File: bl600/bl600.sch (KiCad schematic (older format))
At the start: 27 parts, among them IC1 BL600, IC2 LK112, P1 CONN_4, P2 CONN_3X2, P4 CONN_2, P5 CONN_8, P6 CONN_8, P7 CONN_6X2, Q1 MOSFET_P, Q2 MOSFET_P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

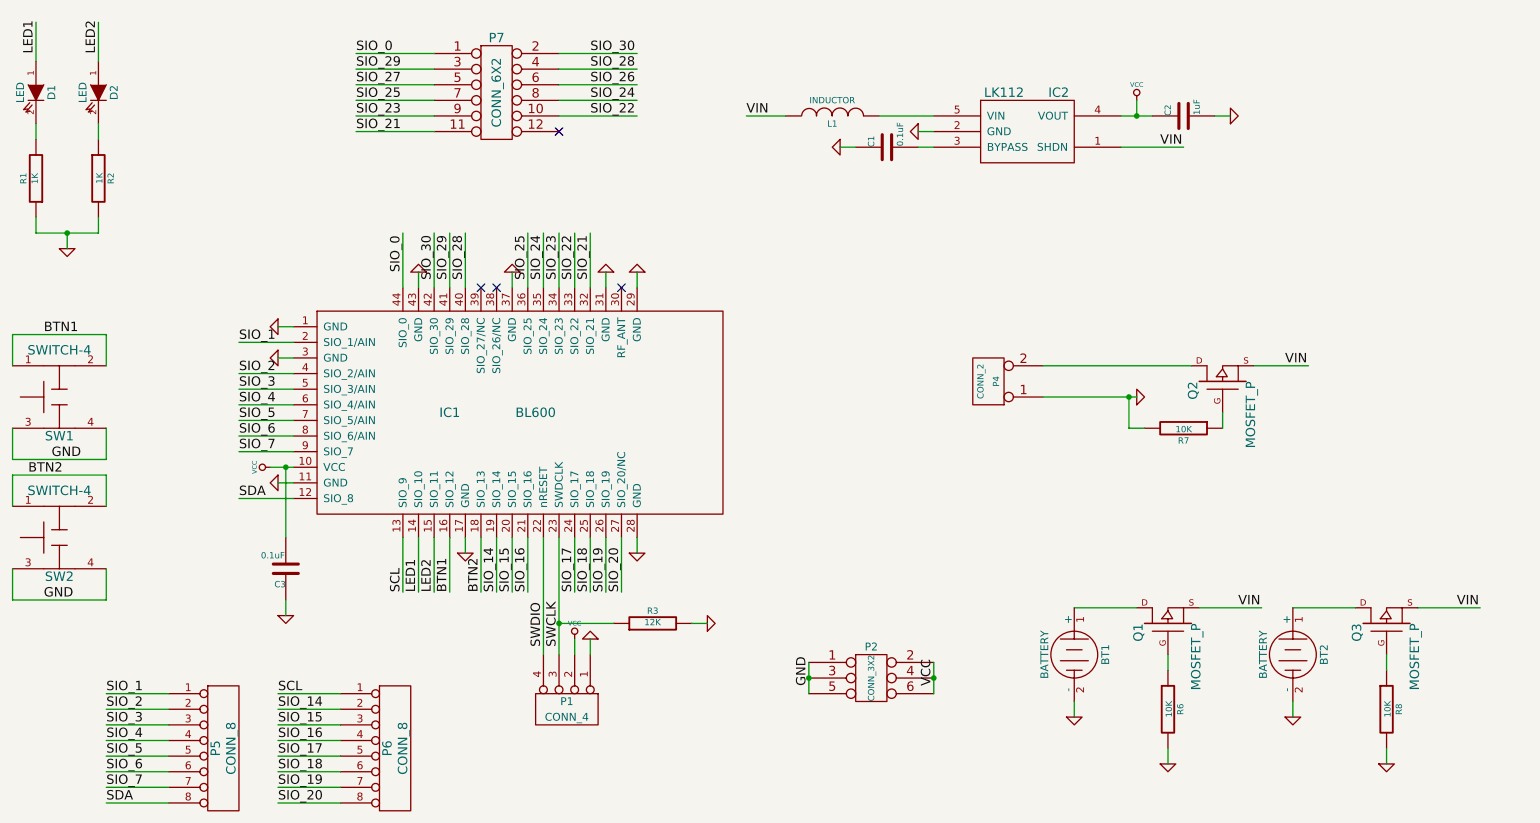
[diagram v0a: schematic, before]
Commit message: BL600 add ARM 10/9 pin SWD header
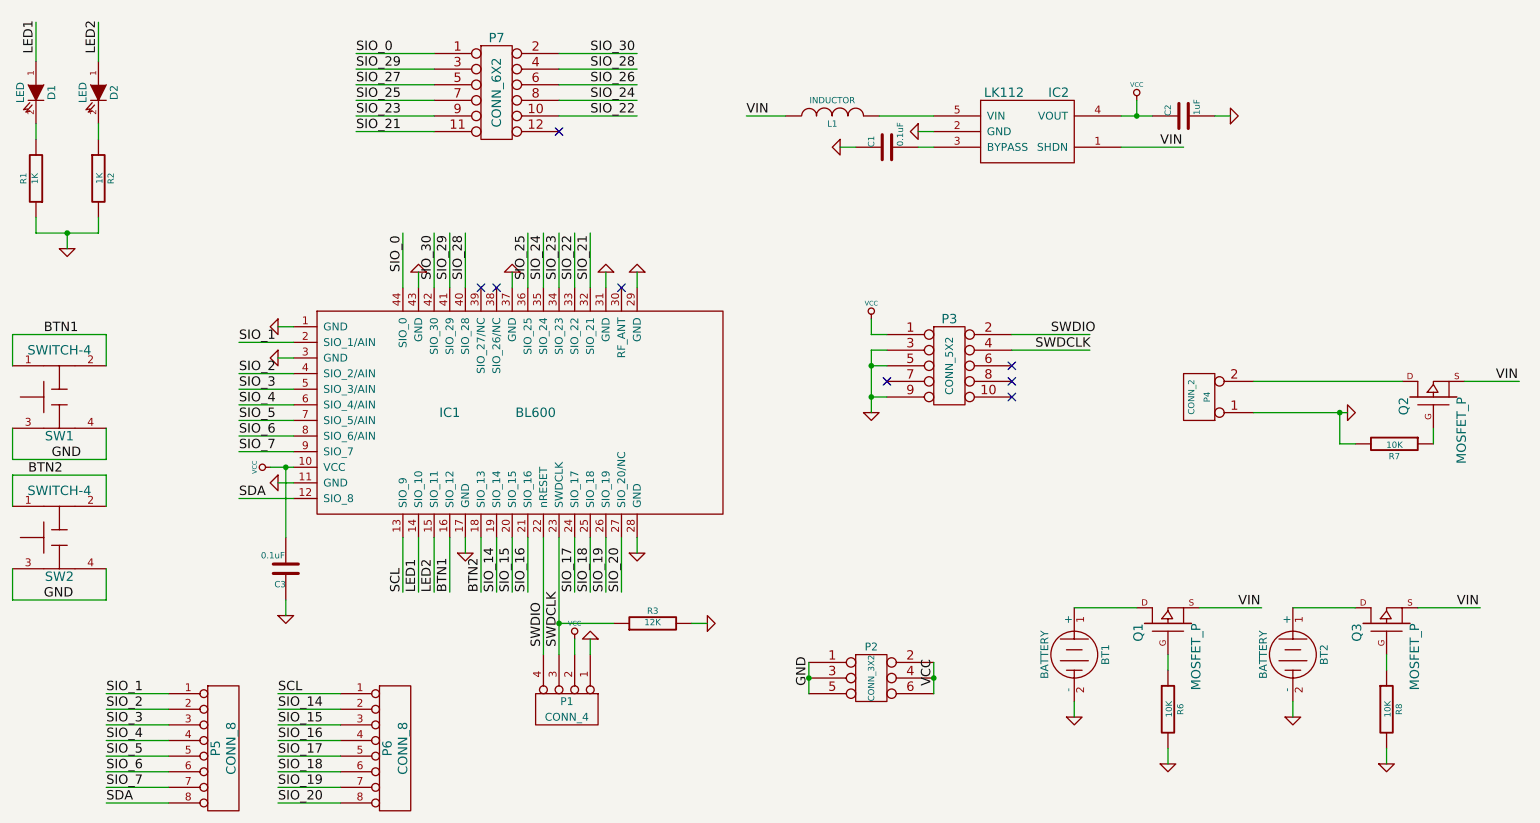
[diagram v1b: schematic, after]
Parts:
- added P3: CONN_5X2, ~, symbol CONN_5X2
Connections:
- net labels added: SWDCLK
- net labels removed: SWCLK
- wire segments 121 -> 129
- no-connect marks 4 -> 8
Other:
- moved on the sheet: P4, Q2, R7
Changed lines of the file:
@@
-EESchema Schematic File Version 2  date Thu 09 May 2013 07:33:31 AM EDT
+EESchema Schematic File Version 2  date Fri 10 May 2013 12:45:30 PM EDT
 LIBS:guan
 LIBS:power
@@
 Sheet 1 1
 Title ""
-Date "13 may 2013"
+Date "10 may 2013"
 Rev ""
 Comp ""
@@
 SWDIO
 Text Label 4700 5200 1    60   ~ 0
-SWCLK
+SWDCLK
 $Comp
 L VCC #PWR09
@@
 L CONN_2 P4
 U 1 1 518C10E5
-P 7450 3500
-F 0 "P4" V 7400 3500 40  0000 C CNN
-F 1 "CONN_2" V 7500 3500 40  0000 C CNN
-F 2 "~" H 7450 3500 60  0000 C CNN
-F 3 "~" H 7450 3500 60  0000 C CNN
-	1    7450 3500
+P 8800 3600
+F 0 "P4" V 8750 3600 40  0000 C CNN
+F 1 "CONN_2" V 8850 3600 40  0000 C CNN
+F 2 "~" H 8800 3600 60  0000 C CNN
+F 3 "~" H 8800 3600 60  0000 C CNN
+	1    8800 3600
 	-1   0    0    1
 $EndComp
@@
 L MOSFET_P Q2
 U 1 1 518C1103
-P 8950 3500
-F 0 "Q2" H 8950 3690 60  0000 R CNN
-F 1 "MOSFET_P" H 8950 3320 60  0000 R CNN
-F 2 "~" H 8950 3500 60  0000 C CNN
-F 3 "~" H 8950 3500 60  0000 C CNN
-	1    8950 3500
+P 10300 3600
+F 0 "Q2" H 10300 3790 60  0000 R CNN
+F 1 "MOSFET_P" H 10300 3420 60  0000 R CNN
+F 2 "~" H 10300 3600 60  0000 C CNN
+F 3 "~" H 10300 3600 60  0000 C CNN
+	1    10300 3600
 	0    -1   -1   0
 $EndComp
-Text Label 9350 3400 0    60   ~ 0
+Text Label 10700 3500 0    60   ~ 0
 VIN
 $Comp
 L GND #PWR014
 U 1 1 518C1EEF
-P 8400 3600
-F 0 "#PWR014" H 8400 3600 30  0001 C CNN
-F 1 "GND" H 8400 3530 30  0001 C CNN
-F 2 "" H 8400 3600 60  0000 C CNN
-F 3 "" H 8400 3600 60  0000 C CNN
-	1    8400 3600
+P 9750 3700
+F 0 "#PWR014" H 9750 3700 30  0001 C CNN
+F 1 "GND" H 9750 3630 30  0001 C CNN
+F 2 "" H 9750 3700 60  0000 C CNN
+F 3 "" H 9750 3700 60  0000 C CNN
+	1    9750 3700
 	0    -1   -1   0
 $EndComp
@@
 L R R7
 U 1 1 518C1F18
-P 8700 3800
-F 0 "R7" V 8780 3800 40  0000 C CNN
-F 1 "10K" V 8707 3801 40  0000 C CNN
-F 2 "~" V 8630 3800 30  0000 C CNN
-F 3 "~" H 8700 3800 30  0000 C CNN
-	1    8700 3800
+P 10050 3900
+F 0 "R7" V 10130 3900 40  0000 C CNN
+F 1 "10K" V 10057 3901 40  0000 C CNN
+F 2 "~" V 9980 3900 30  0000 C CNN
+F 3 "~" H 10050 3900 30  0000 C CNN
+	1    10050 3900
 	0    1    1    0
 $EndComp
@@
 	8000 5650 8000 5550
 Wire Wire Line
-	7800 3400 8750 3400
-Wire Wire Line
-	9150 3400 9500 3400
-Wire Wire Line
-	7800 3600 8400 3600
-Wire Wire Line
-	8950 3700 8950 3800
-Wire Wire Line
-	8450 3800 8350 3800
-Wire Wire Line
-	8350 3800 8350 3600
-Connection ~ 8350 3600
+	9150 3500 10100 3500
+Wire Wire Line
+	10500 3500 10850 3500
+Wire Wire Line
+	9150 3700 9750 3700
+Wire Wire Line
+	10300 3800 10300 3900
+Wire Wire Line
+	9800 3900 9700 3900
+Wire Wire Line
+	9700 3900 9700 3700
+Connection ~ 9700 3700
 Wire Wire Line
 	8000 4950 8400 4950
@@
 NoConn ~ 4200 2900
 NoConn ~ 4300 2900
+$Comp
+L CONN_5X2 P3
+U 1 1 518C242E
+P 7200 3400
+F 0 "P3" H 7200 3700 60  0000 C CNN
+F 1 "CONN_5X2" V 7200 3400 50  0000 C CNN
+F 2 "~" H 7200 3400 60  0000 C CNN
+F 3 "~" H 7200 3400 60  0000 C CNN
+	1    7200 3400
+	1    0    0    -1
+$EndComp
+$Comp
+L VCC #PWR025
+U 1 1 518C3106
+P 6700 3100
+F 0 "#PWR025" H 6700 3200 30  0001 C CNN
+F 1 "VCC" H 6700 3200 30  0000 C CNN
+F 2 "" H 6700 3100 60  0000 C CNN
+F 3 "" H 6700 3100 60  0000 C CNN
+	1    6700 3100
+	1    0    0    -1
+$EndComp
+Wire Wire Line
+	6700 3100 6700 3200
+Wire Wire Line
+	6700 3200 6800 3200
+$Comp
+L GND #PWR026
+U 1 1 518C3196
+P 6700 3700
+F 0 "#PWR026" H 6700 3700 30  0001 C CNN
+F 1 "GND" H 6700 3630 30  0001 C CNN
+F 2 "" H 6700 3700 60  0000 C CNN
+F 3 "" H 6700 3700 60  0000 C CNN
+	1    6700 3700
+	1    0    0    -1
+$EndComp
+Wire Wire Line
+	6700 3700 6700 3300
+Wire Wire Line
+	6700 3300 6800 3300
+Wire Wire Line
+	6800 3400 6700 3400
+Connection ~ 6700 3400
+Wire Wire Line
+	6800 3600 6700 3600
+Connection ~ 6700 3600
+NoConn ~ 6800 3500
+Wire Wire Line
+	7600 3200 8100 3200
+Wire Wire Line
+	8100 3300 7600 3300
+Text Label 7850 3200 0    60   ~ 0
+SWDIO
+Text Label 7750 3300 0    60   ~ 0
+SWDCLK
+NoConn ~ 7600 3400
+NoConn ~ 7600 3500
+NoConn ~ 7600 3600
 $EndSCHEMATC

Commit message: Connect CR2032 holder directly to 3V3
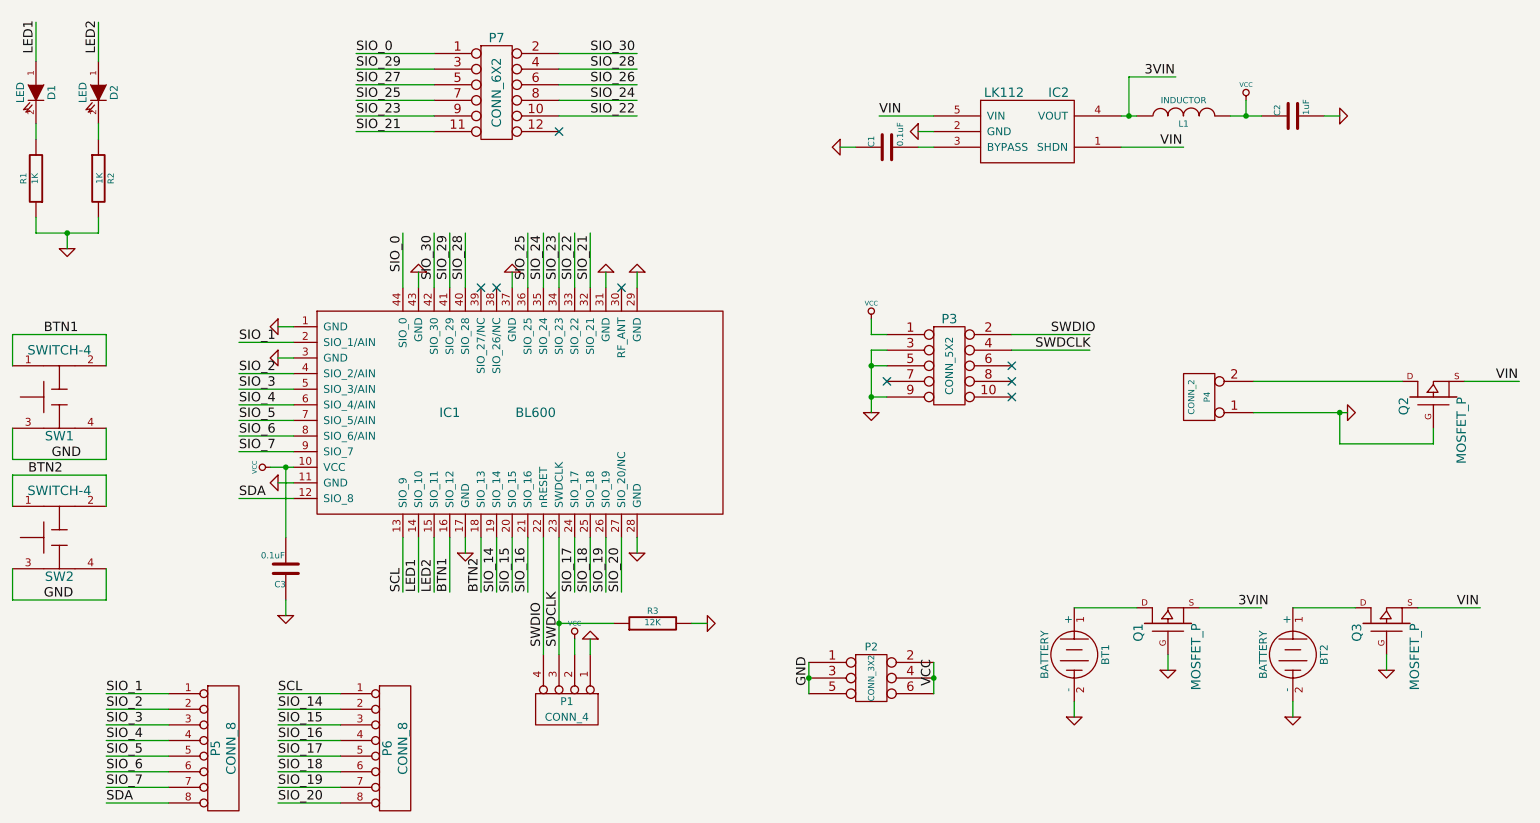
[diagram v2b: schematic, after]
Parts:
- removed R6, R7, R8: 10K, ~, symbol R
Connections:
- net labels added: 3VIN
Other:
- moved on the sheet: C2, L1
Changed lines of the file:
@@
-EESchema Schematic File Version 2  date Fri 10 May 2013 12:45:30 PM EDT
+EESchema Schematic File Version 2  date Tue 14 May 2013 06:35:55 AM EDT
 LIBS:guan
 LIBS:power
@@
 Sheet 1 1
 Title ""
-Date "10 may 2013"
+Date "14 may 2013"
 Rev ""
 Comp ""
@@
 $EndComp
 $Comp
-L R R7
-U 1 1 518C1F18
-P 10050 3900
-F 0 "R7" V 10130 3900 40  0000 C CNN
-F 1 "10K" V 10057 3901 40  0000 C CNN
-F 2 "~" V 9980 3900 30  0000 C CNN
-F 3 "~" H 10050 3900 30  0000 C CNN
-	1    10050 3900
-	0    1    1    0
-$EndComp
-$Comp
 L MOSFET_P Q1
 U 1 1 518C2D3A
@@
 $EndComp
 Text Label 9050 4950 0    60   ~ 0
-VIN
-$Comp
-L R R6
-U 1 1 518C2D95
-P 8600 5600
-F 0 "R6" V 8680 5600 40  0000 C CNN
-F 1 "10K" V 8607 5601 40  0000 C CNN
-F 2 "~" V 8530 5600 30  0000 C CNN
-F 3 "~" H 8600 5600 30  0000 C CNN
-	1    8600 5600
-	1    0    0    -1
-$EndComp
-$Comp
-L GND #PWR015
-U 1 1 518C2DCB
-P 8600 5950
-F 0 "#PWR015" H 8600 5950 30  0001 C CNN
-F 1 "GND" H 8600 5880 30  0001 C CNN
-F 2 "" H 8600 5950 60  0000 C CNN
-F 3 "" H 8600 5950 60  0000 C CNN
-	1    8600 5950
-	1    0    0    -1
-$EndComp
+3VIN
 $Comp
 L BATTERY BT2
@@
 $EndComp
 $Comp
-L GND #PWR016
+L GND #PWR015
 U 1 1 518C5850
 P 9400 5650
-F 0 "#PWR016" H 9400 5650 30  0001 C CNN
+F 0 "#PWR015" H 9400 5650 30  0001 C CNN
 F 1 "GND" H 9400 5580 30  0001 C CNN
 F 2 "" H 9400 5650 60  0000 C CNN
@@
 VIN
 $Comp
-L R R8
-U 1 1 518C5860
-P 10000 5600
-F 0 "R8" V 10080 5600 40  0000 C CNN
-F 1 "10K" V 10007 5601 40  0000 C CNN
-F 2 "~" V 9930 5600 30  0000 C CNN
-F 3 "~" H 10000 5600 30  0000 C CNN
-	1    10000 5600
-	1    0    0    -1
-$EndComp
-$Comp
-L GND #PWR017
-U 1 1 518C5867
-P 10000 5950
-F 0 "#PWR017" H 10000 5950 30  0001 C CNN
-F 1 "GND" H 10000 5880 30  0001 C CNN
-F 2 "" H 10000 5950 60  0000 C CNN
-F 3 "" H 10000 5950 60  0000 C CNN
-	1    10000 5950
-	1    0    0    -1
-$EndComp
-$Comp
 L LK112 IC2
 U 1 1 518C5930
@@
 $EndComp
 $Comp
-L VCC #PWR018
+L VCC #PWR016
 U 1 1 518C593F
-P 8400 1700
-F 0 "#PWR018" H 8400 1800 30  0001 C CNN
-F 1 "VCC" H 8400 1800 30  0000 C CNN
-F 2 "" H 8400 1700 60  0000 C CNN
-F 3 "" H 8400 1700 60  0000 C CNN
-	1    8400 1700
+P 9100 1700
+F 0 "#PWR016" H 9100 1800 30  0001 C CNN
+F 1 "VCC" H 9100 1800 30  0000 C CNN
+F 2 "" H 9100 1700 60  0000 C CNN
+F 3 "" H 9100 1700 60  0000 C CNN
+	1    9100 1700
 	1    0    0    -1
 $EndComp
@@
 L C C2
 U 1 1 518C5975
-P 8700 1800
-F 0 "C2" H 8700 1900 40  0000 L CNN
-F 1 "1uF" H 8706 1715 40  0000 L CNN
-F 2 "~" H 8738 1650 30  0000 C CNN
-F 3 "~" H 8700 1800 60  0000 C CNN
-	1    8700 1800
+P 9400 1800
+F 0 "C2" H 9400 1900 40  0000 L CNN
+F 1 "1uF" H 9406 1715 40  0000 L CNN
+F 2 "~" H 9438 1650 30  0000 C CNN
+F 3 "~" H 9400 1800 60  0000 C CNN
+	1    9400 1800
 	0    -1   -1   0
 $EndComp
 $Comp
-L GND #PWR019
+L GND #PWR017
 U 1 1 518C59BC
-P 9000 1800
-F 0 "#PWR019" H 9000 1800 30  0001 C CNN
-F 1 "GND" H 9000 1730 30  0001 C CNN
-F 2 "" H 9000 1800 60  0000 C CNN
-F 3 "" H 9000 1800 60  0000 C CNN
-	1    9000 1800
+P 9700 1800
+F 0 "#PWR017" H 9700 1800 30  0001 C CNN
+F 1 "GND" H 9700 1730 30  0001 C CNN
+F 2 "" H 9700 1800 60  0000 C CNN
+F 3 "" H 9700 1800 60  0000 C CNN
+	1    9700 1800
 	0    -1   -1   0
 $EndComp
@@
 $EndComp
 $Comp
-L GND #PWR020
+L GND #PWR018
 U 1 1 518C6713
 P 7000 1900
-F 0 "#PWR020" H 7000 1900 30  0001 C CNN
+F 0 "#PWR018" H 7000 1900 30  0001 C CNN
 F 1 "GND" H 7000 1830 30  0001 C CNN
 F 2 "" H 7000 1900 60  0000 C CNN
@@
 $EndComp
 $Comp
-L GND #PWR021
+L GND #PWR019
 U 1 1 518C677B
 P 6500 2000
-F 0 "#PWR021" H 6500 2000 30  0001 C CNN
+F 0 "#PWR019" H 6500 2000 30  0001 C CNN
 F 1 "GND" H 6500 1930 30  0001 C CNN
 F 2 "" H 6500 2000 60  0000 C CNN
@@
 	0    1    1    0
 $EndComp
-Text Label 5900 1800 0    60   ~ 0
-VIN
 Text Label 3800 4850 1    60   ~ 0
 LED1
@@
 SIO_21
 $Comp
-L GND #PWR022
+L GND #PWR020
 U 1 1 518CAE3B
 P 2900 3350
-F 0 "#PWR022" H 2900 3350 30  0001 C CNN
+F 0 "#PWR020" H 2900 3350 30  0001 C CNN
 F 1 "GND" H 2900 3280 30  0001 C CNN
 F 2 "" H 2900 3350 60  0000 C CNN
@@
 $EndComp
 $Comp
-L GND #PWR023
+L GND #PWR021
 U 1 1 518CD8CF
 P 1550 2650
-F 0 "#PWR023" H 1550 2650 30  0001 C CNN
+F 0 "#PWR021" H 1550 2650 30  0001 C CNN
 F 1 "GND" H 1550 2580 30  0001 C CNN
 F 2 "" H 1550 2650 60  0000 C CNN
@@
 L INDUCTOR L1
 U 1 1 518D06C6
-P 6450 1800
-F 0 "L1" V 6400 1800 40  0000 C CNN
-F 1 "INDUCTOR" V 6550 1800 40  0000 C CNN
-F 2 "~" H 6450 1800 60  0000 C CNN
-F 3 "~" H 6450 1800 60  0000 C CNN
-	1    6450 1800
+P 8700 1800
+F 0 "L1" V 8650 1800 40  0000 C CNN
+F 1 "INDUCTOR" V 8800 1800 40  0000 C CNN
+F 2 "~" H 8700 1800 60  0000 C CNN
+F 3 "~" H 8700 1800 60  0000 C CNN
+	1    8700 1800
 	0    -1   -1   0
 $EndComp
@@
 	9150 3700 9750 3700
 Wire Wire Line
-	10300 3800 10300 3900
-Wire Wire Line
-	9800 3900 9700 3900
+	9700 3900 10300 3900
 Wire Wire Line
 	9700 3900 9700 3700
@@
 	8600 5350 8600 5250
 Wire Wire Line
-	8600 5950 8600 5850
-Wire Wire Line
 	9400 5650 9400 5550
 Wire Wire Line
@@
 	10000 5350 10000 5250
 Wire Wire Line
-	10000 5950 10000 5850
-Wire Wire Line
-	8300 1800 8500 1800
-Wire Wire Line
-	8400 1800 8400 1700
-Connection ~ 8400 1800
-Wire Wire Line
-	9000 1800 8900 1800
+	9000 1800 9200 1800
+Wire Wire Line
+	9100 1800 9100 1700
+Connection ~ 9100 1800
+Wire Wire Line
+	9700 1800 9600 1800
 Wire Wire Line
 	8300 2000 8700 2000
@@
 	1750 2550 1750 2450
 Connection ~ 1550 2550
-Wire Wire Line
-	6150 1800 5900 1800
 Wire Wire Line
 	3400 1400 3900 1400
@@
 Connection ~ 2950 4050
 $Comp
-L GND #PWR024
+L GND #PWR022
 U 1 1 51906D8F
 P 2950 5000
-F 0 "#PWR024" H 2950 5000 30  0001 C CNN
+F 0 "#PWR022" H 2950 5000 30  0001 C CNN
 F 1 "GND" H 2950 4930 30  0001 C CNN
 F 2 "" H 2950 5000 60  0000 C CNN
@@
 $EndComp
 $Comp
-L VCC #PWR025
+L VCC #PWR023
 U 1 1 518C3106
 P 6700 3100
-F 0 "#PWR025" H 6700 3200 30  0001 C CNN
+F 0 "#PWR023" H 6700 3200 30  0001 C CNN
 F 1 "VCC" H 6700 3200 30  0000 C CNN
 F 2 "" H 6700 3100 60  0000 C CNN
@@
 	6700 3200 6800 3200
 $Comp
-L GND #PWR026
+L GND #PWR024
 U 1 1 518C3196
 P 6700 3700
-F 0 "#PWR026" H 6700 3700 30  0001 C CNN
+F 0 "#PWR024" H 6700 3700 30  0001 C CNN
 F 1 "GND" H 6700 3630 30  0001 C CNN
 F 2 "" H 6700 3700 60  0000 C CNN
@@
 NoConn ~ 7600 3500
 NoConn ~ 7600 3600
+Text Label 6750 1800 0    60   ~ 0
+VIN
+Wire Wire Line
+	8300 1800 8400 1800
+Wire Wire Line
+	8350 1800 8350 1550
+Wire Wire Line
+	8350 1550 8650 1550
+Connection ~ 8350 1800
+Text Label 8450 1550 0    60   ~ 0
+3VIN
+$Comp
+L GND #PWR025
+U 1 1 5191BF02
+P 8600 5350
+F 0 "#PWR025" H 8600 5350 30  0001 C CNN
+F 1 "GND" H 8600 5280 30  0001 C CNN
+F 2 "" H 8600 5350 60  0000 C CNN
+F 3 "" H 8600 5350 60  0000 C CNN
+	1    8600 5350
+	1    0    0    -1
+$EndComp
+$Comp
+L GND #PWR026
+U 1 1 5191BF11
+P 10000 5350
+F 0 "#PWR026" H 10000 5350 30  0001 C CNN
+F 1 "GND" H 10000 5280 30  0001 C CNN
+F 2 "" H 10000 5350 60  0000 C CNN
+F 3 "" H 10000 5350 60  0000 C CNN
+	1    10000 5350
+	1    0    0    -1
+$EndComp
+Wire Wire Line
+	10300 3900 10300 3800
 $EndSCHEMATC
